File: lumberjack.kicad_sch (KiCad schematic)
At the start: 162 parts, among them J1 USB_B_Mini, SW1 RESET, SW2 BOOT, U2 ATmega32A-P, Y1 16MHz

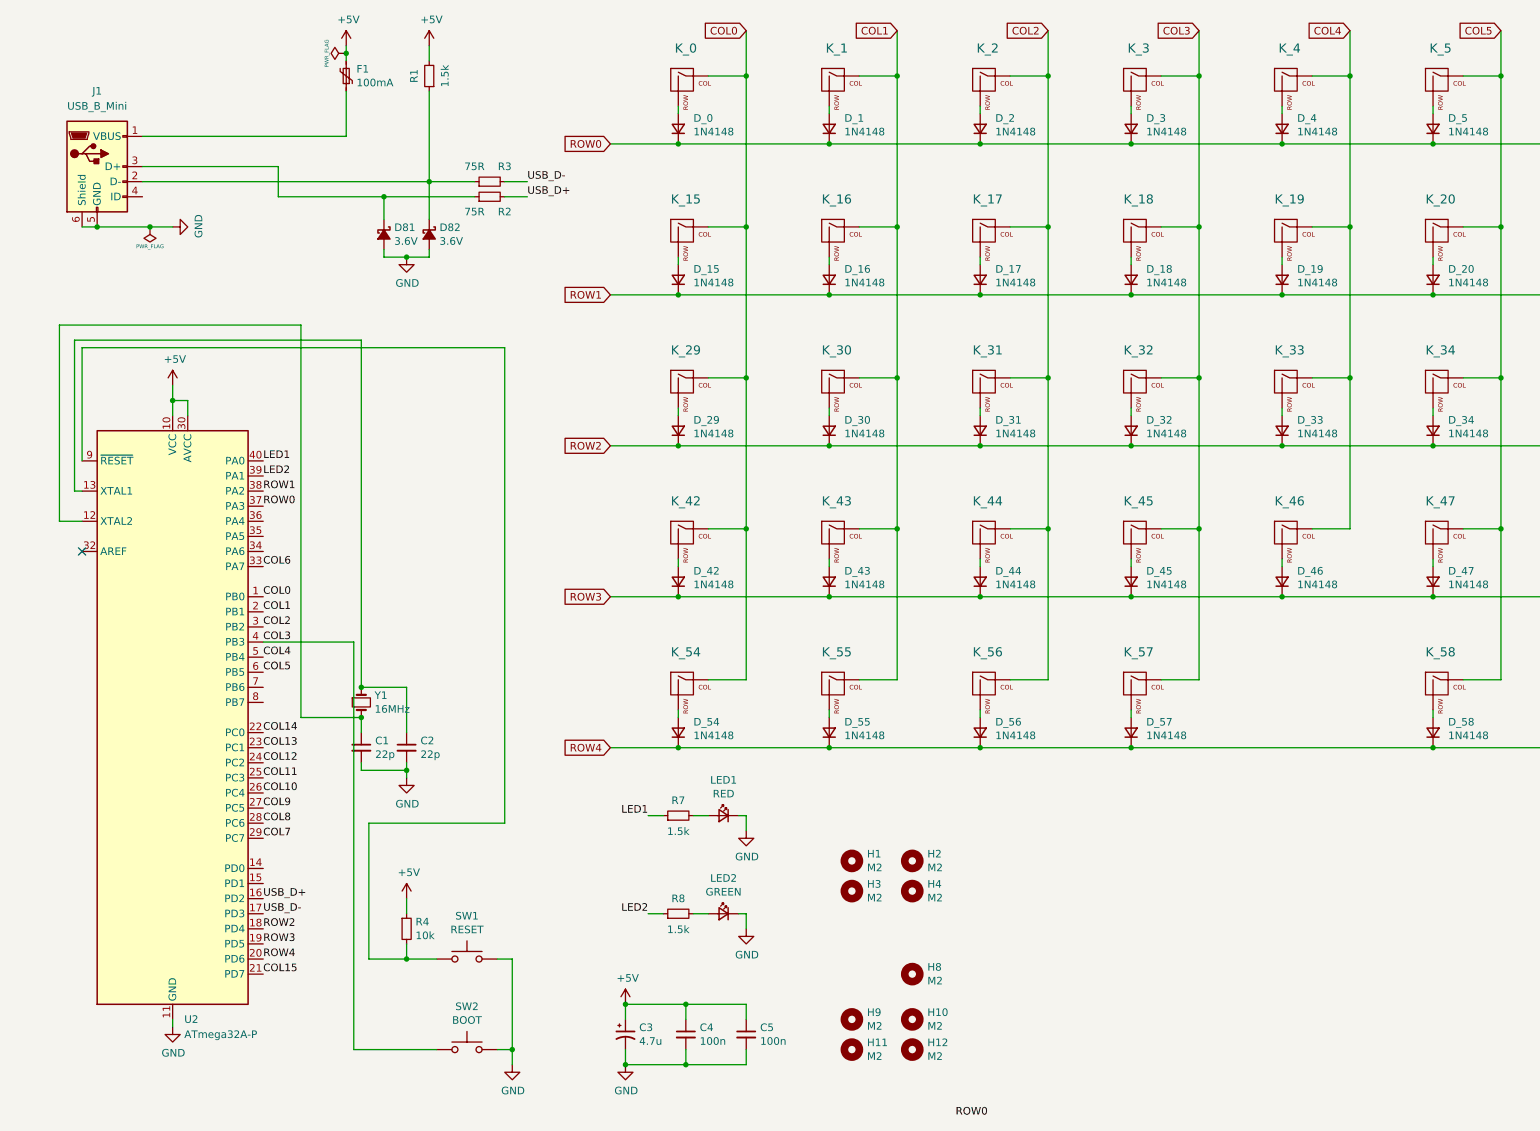
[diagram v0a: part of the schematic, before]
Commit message: replace mcu with teensy
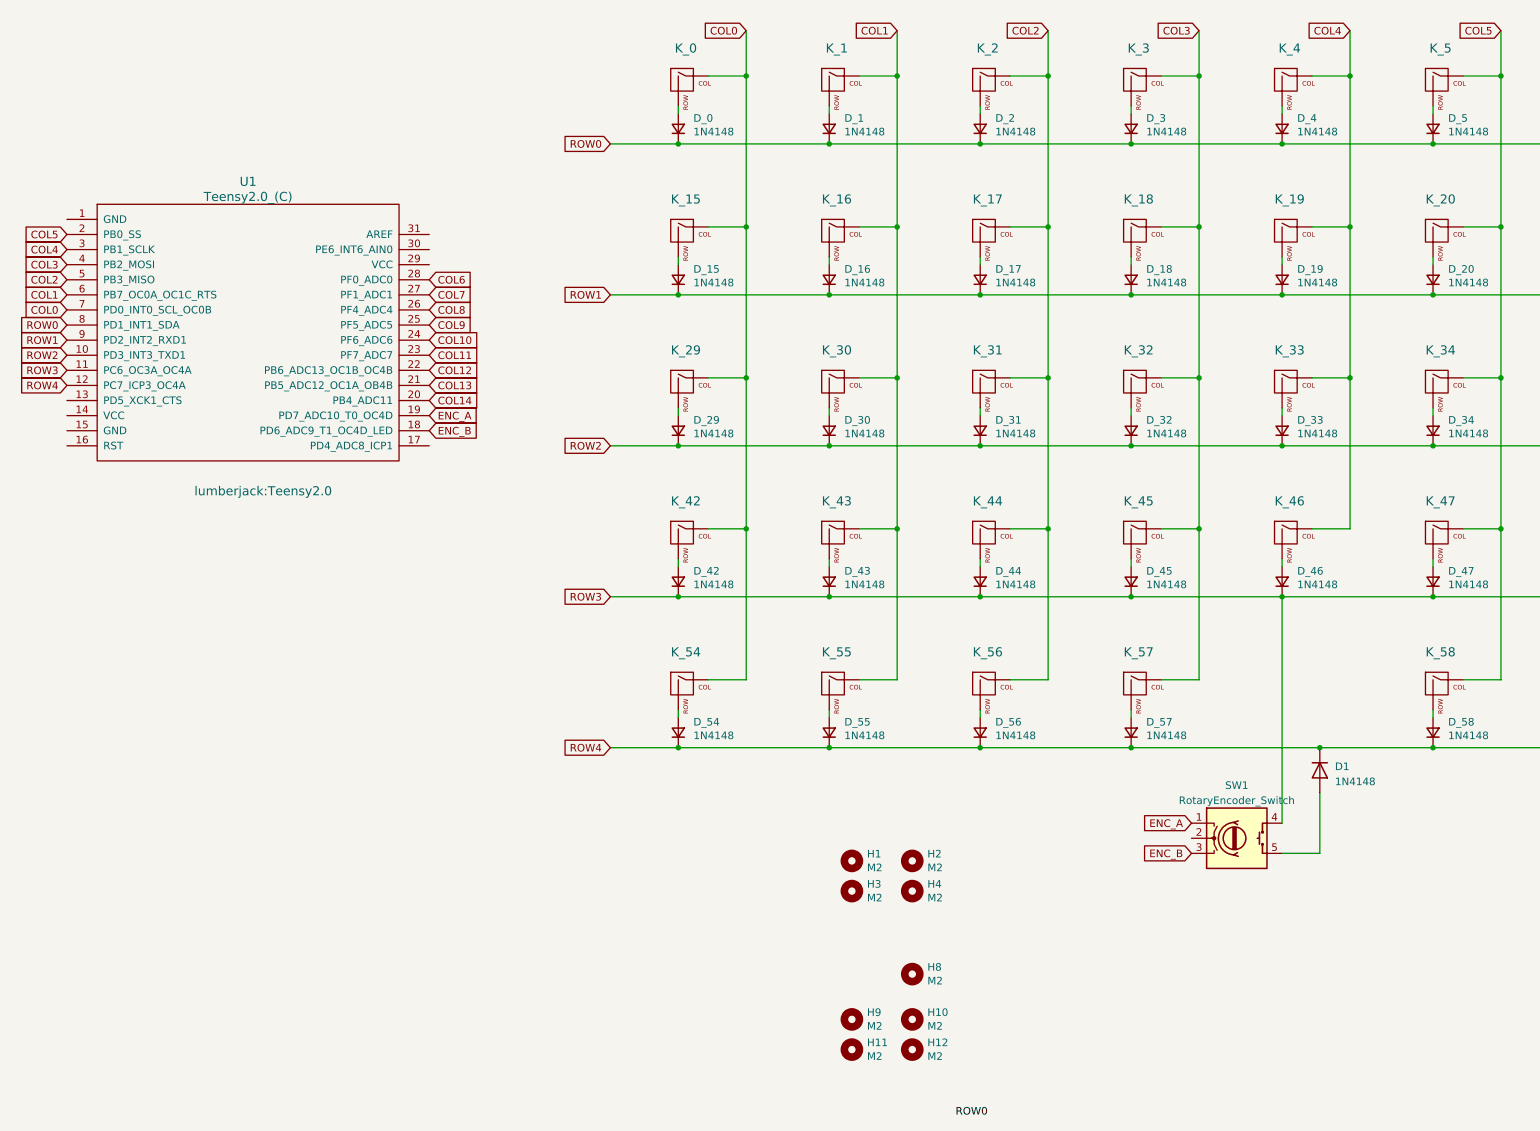
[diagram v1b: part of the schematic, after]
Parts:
- removed C1, C2: 22p, Capacitor_THT:C_Disc_D3.0mm_W1.6mm_P2.50mm, symbol Device:C_Small
- removed C3: 4.7u, Capacitor_THT:CP_Radial_D4.0mm_P1.50mm, symbol lumberjack-rescue:CP1_Small-Device
- removed C4, C5: 100n, Capacitor_THT:C_Disc_D4.3mm_W1.9mm_P5.00mm, symbol Device:C_Small
- removed D81, D82: 3.6V, Diode_THT:D_DO-35_SOD27_P7.62mm_Horizontal, symbol lumberjack-rescue:D_Schottky_Small_ALT-Device
- removed F1: 100mA, Fuse:Fuse_Bourns_MF-RHT100, symbol Device:Polyfuse_Small
- removed J1: USB_B_Mini, lumberjack:USB_Mini-B, symbol Connector:USB_B_Mini
- removed LED1: RED, LED_THT:LED_D3.0mm, symbol Device:LED_Small
- removed LED2: GREEN, LED_THT:LED_D3.0mm, symbol Device:LED_Small
- removed R1, R7, R8: 1.5k, Resistor_THT:R_Axial_DIN0204_L3.6mm_D1.6mm_P7.62mm_Horizontal, symbol Device:R_Small
- removed R2, R3: 75R, Resistor_THT:R_Axial_DIN0204_L3.6mm_D1.6mm_P7.62mm_Horizontal, symbol Device:R_Small
- removed R4: 10k, Resistor_THT:R_Axial_DIN0204_L3.6mm_D1.6mm_P7.62mm_Horizontal, symbol Device:R_Small
- removed SW1: RESET, Button_Switch_THT:SW_PUSH_6mm, symbol Switch:SW_Push
- removed SW2: BOOT, Button_Switch_THT:SW_PUSH_6mm, symbol Switch:SW_Push
- removed U2: ATmega32A-P, Package_DIP:DIP-40_W15.24mm, symbol MCU_Microchip_ATmega:ATmega32A-P
- removed Y1: 16MHz, Crystal:Crystal_HC49-4H_Vertical, symbol Device:Crystal_Small
- added D1: 1N4148, Diode_THT:D_DO-35_SOD27_P7.62mm_Horizontal, symbol Diode:1N4148
- added SW1: RotaryEncoder_Switch, Potentiometer_THT:Potentiometer_Bourns_PTV09A-1_Single_Vertical, symbol Device:RotaryEncoder_Switch
- added U1: Teensy2.0_(C), lumberjack:Teensy2.0, symbol teensy:Teensy2.0_(C)
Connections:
- net COL0: now also U1.7 (PD0_INT0_SCL_OC0B)
- net COL1: now also U1.6 (PB7_OC0A_OC1C_RTS)
- net COL10: now also U1.24 (PF6_ADC6)
- net COL11: now also U1.23 (PF7_ADC7)
- net COL12: now also U1.22 (PB6_ADC13_OC1B_OC4B)
- net COL13: now also U1.21 (PB5_ADC12_OC1A_OB4B)
- net COL14: now also U1.20 (PB4_ADC11)
- net COL2: now also U1.5 (PB3_MISO)
- net COL3: now also U1.4 (PB2_MOSI)
- net COL4: now also U1.3 (PB1_SCLK)
- net COL5: now also U1.2 (PB0_SS)
- net COL6: now also U1.28 (PF0_ADC0)
- net COL7: now also U1.27 (PF1_ADC1)
- net COL8: now also U1.26 (PF4_ADC4)
- net COL9: now also U1.25 (PF5_ADC5)
- net ROW0: now also U1.8 (PD1_INT1_SDA)
- net ROW1: now also U1.9 (PD2_INT2_RXD1)
- net ROW2: now also U1.10 (PD3_INT3_TXD1)
- net ROW3: now also SW1.4, U1.11 (PC6_OC3A_OC4A)
- net ROW4: now also D1.1 (K), U1.12 (PC7_ICP3_OC4A)
- new net: D1.2 (A), SW1.5
- new net ENC_A: SW1.1, U1.19 (PD7_ADC10_T0_OC4D)
- new net ENC_B: SW1.3, U1.18 (PD6_ADC9_T1_OC4D_LED)
- no-connect marks 1 -> 0

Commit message: add cirque trackpad
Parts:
- removed D1: 1N4148, Diode_THT:D_DO-35_SOD27_P7.62mm_Horizontal, symbol Diode:1N4148
- removed SW1: RotaryEncoder_Switch, Potentiometer_THT:Potentiometer_Bourns_PTV09A-1_Single_Vertical, symbol Device:RotaryEncoder_Switch
- added D_57 (x2): 1N4148, Diode_THT:D_DO-35_SOD27_P7.62mm_Horizontal, symbol Device:D_Small
- added H10, H11, H12, H13, H14: M2, lumberjack:MountingHole_M2, symbol Mechanical:MountingHole
- added K_57 (x2): KEYSW, Button_Switch_Keyboard:SW_Cherry_MX_1.75u_PCB, symbol MX_Alps_Hybrid:MX-NoLED
- added U2: Cirque40mm, lumberjack:cirque_40mm, symbol cirque:40mm_cirque_trackpad
- K_58, K_59: footprint Button_Switch_Keyboard:SW_Cherry_MX_1.75u_PCB -> Button_Switch_Keyboard:SW_Cherry_MX_1.00u_PCB
- renumbered H8 to H5, H9 to H6, H10 to H7, H11 to H8, H12 to H9
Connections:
- net COL0: now also U1.2 (PB0_SS); no longer U1.7 (PD0_INT0_SCL_OC0B)
- net COL1: now also U1.3 (PB1_SCLK); no longer U1.6 (PB7_OC0A_OC1C_RTS)
- net COL11: now also U1.25 (PF5_ADC5); no longer U1.23 (PF7_ADC7)
- net COL12: now also U1.26 (PF4_ADC4); no longer U1.22 (PB6_ADC13_OC1B_OC4B)
- net COL13: now also U1.27 (PF1_ADC1); no longer U1.21 (PB5_ADC12_OC1A_OB4B)
- net COL14: now also U1.28 (PF0_ADC0); no longer U1.20 (PB4_ADC11)
- net COL2: now also U1.4 (PB2_MOSI); no longer U1.5 (PB3_MISO)
- net COL3: now also U1.5 (PB3_MISO); no longer U1.4 (PB2_MOSI)
- net COL4: now also U1.6 (PB7_OC0A_OC1C_RTS), K_57.1 (COL); no longer U1.3 (PB1_SCLK)
- net COL5: now also U1.9 (PD2_INT2_RXD1); no longer U1.2 (PB0_SS)
- net COL6: now also U1.20 (PB4_ADC11); no longer U1.28 (PF0_ADC0)
- net COL7: now also U1.21 (PB5_ADC12_OC1A_OB4B), K_57.1 (COL); no longer U1.27 (PF1_ADC1)
- net COL8: now also U1.22 (PB6_ADC13_OC1B_OC4B); no longer U1.26 (PF4_ADC4)
- net COL9: now also U1.23 (PF7_ADC7); no longer U1.25 (PF5_ADC5)
- net ROW0: now also U1.10 (PD3_INT3_TXD1); no longer U1.8 (PD1_INT1_SDA)
- net ROW1: now also U1.11 (PC6_OC3A_OC4A); no longer U1.9 (PD2_INT2_RXD1)
- net ROW2: now also U1.12 (PC7_ICP3_OC4A); no longer U1.10 (PD3_INT3_TXD1)
- net ROW3: now also U1.13 (PD5_XCK1_CTS); no longer U1.11 (PC6_OC3A_OC4A)
- net ROW4: now also U1.17 (PD4_ADC8_ICP1), D_57.1 (K), D_57.1 (K); no longer U1.12 (PC7_ICP3_OC4A)
- net at U1.14 (VCC): now also U2.4 (VDD)
- net at U1.15 (GND): now also U2.1 (GND)
- new net: D_57.2 (A), K_57.2 (ROW) (x2)
- new net: U1.7 (PD0_INT0_SCL_OC0B), U2.2 (SCL)
- new net: U1.8 (PD1_INT1_SDA), U2.3 (SDA)
